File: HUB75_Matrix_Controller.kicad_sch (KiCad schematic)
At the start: 61 parts, among them J1 USB_C_Receptacle_USB2.0_16P, J2 Barrel_Jack_MountingPin, J3 Screw_Terminal_01x02, J4 Micro_SD_Card_Det2, J5 SFH11-PBPC-D08-ST-BK, SW1 EN, SW2 BOOT, U1 LSM6DSOTR, U2 AMS1117-3.3, U3 USBLC6-2SC6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

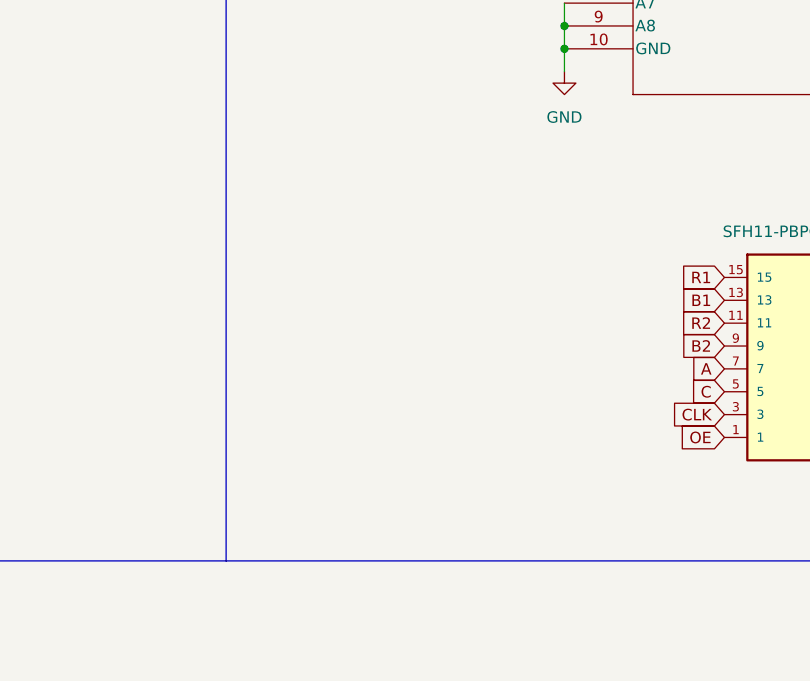
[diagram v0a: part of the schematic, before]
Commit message: ESP -> HUB75
Option to ignore Level Shifter
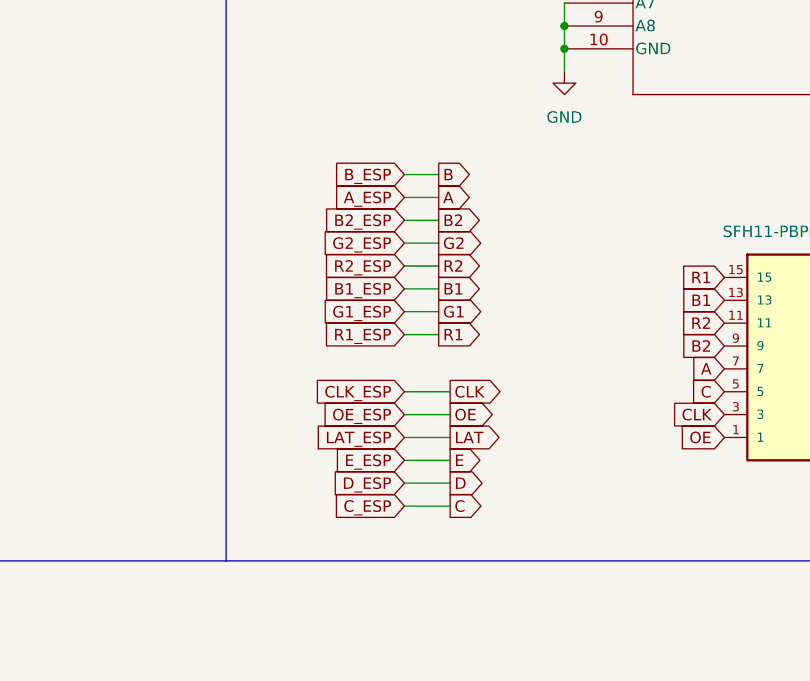
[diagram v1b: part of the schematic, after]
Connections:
- net A_ESP is gone; now on net A: U6.12 (GPIO7/ADC1_CH6), U7.3 (A2)
- net B1_ESP is gone; now on net B1: U6.8 (GPIO3/ADC1_CH2), U7.7 (A6)
- net B2_ESP is gone; now on net B2: U6.11 (GPIO6/ADC1_CH5), U7.4 (A3)
- net B_ESP is gone; now on net B: U6.13 (GPIO8/ADC1_CH7), U7.2 (A1)
- net CLK_ESP is gone; now on net CLK: U6.19 (GPIO14/ADC2_CH3), U8.2 (A1)
- net C_ESP is gone; now on net C: U6.14 (GPIO9/ADC1_CH8), U8.7 (A6)
- net D_ESP is gone; now on net D: U6.15 (GPIO10/ADC1_CH9), U8.6 (A5)
- net E_ESP is gone; now on net E: U6.16 (GPIO11/ADC2_CH0), U8.5 (A4)
- net G1_ESP is gone; now on net G1: U6.7 (GPIO2/ADC1_CH1), U7.8 (A7)
- net G2_ESP is gone; now on net G2: U6.10 (GPIO5/ADC1_CH4), U7.5 (A4)
- net LAT_ESP is gone; now on net LAT: U6.17 (GPIO12/ADC2_CH1), U8.4 (A3)
- net OE_ESP is gone; now on net OE: U6.18 (GPIO13/ADC2_CH2), U8.3 (A2)
- net R1_ESP is gone; now on net R1: U6.6 (GPIO1/ADC1_CH0), U7.9 (A8)
- net R2_ESP is gone; now on net R2: U6.9 (GPIO4/ADC1_CH3), U7.6 (A5)

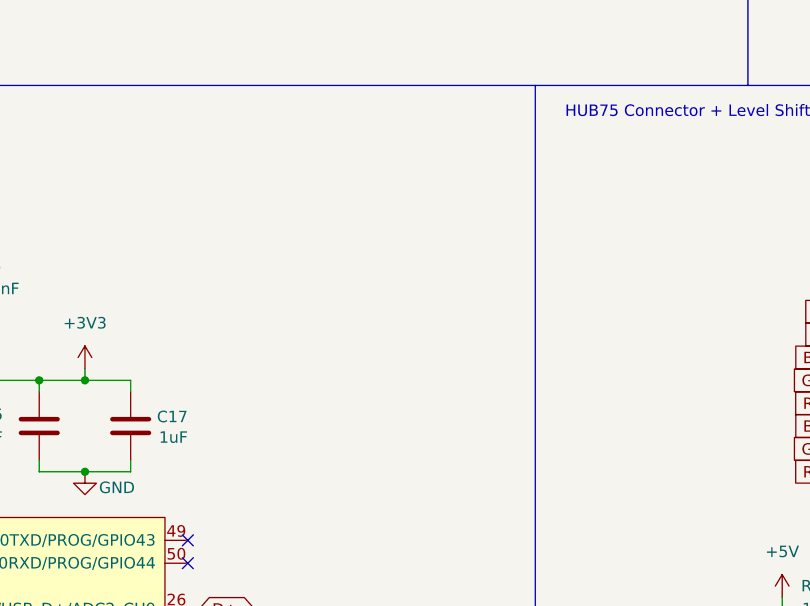
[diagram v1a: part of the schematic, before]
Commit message: Silkscreen Updates
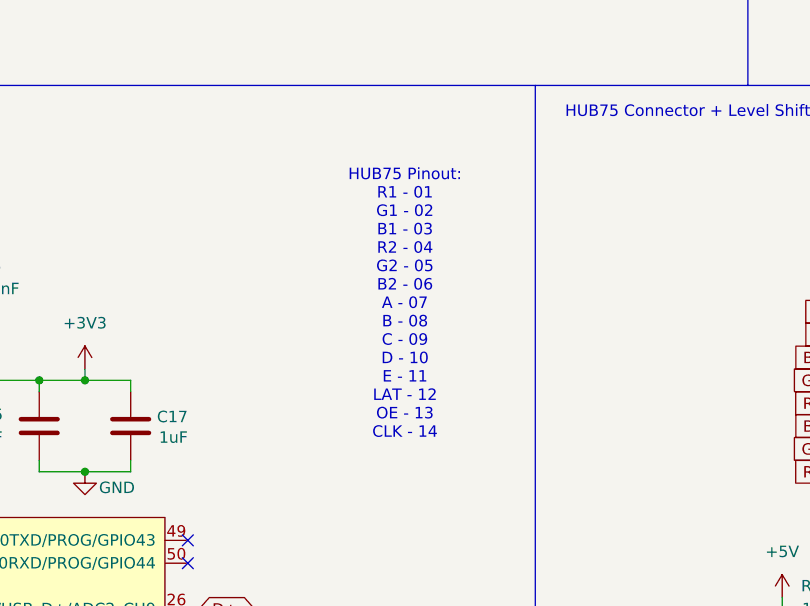
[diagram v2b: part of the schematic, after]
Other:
- note added: "HUB75 Pinout: R1 - 01 G1 - 02 B1 - 03 R2 - 04 G2 - 05 B2 - 06 A - 07 B - 08 C - 09 D - 10 E - 11 LAT - 12 OE - 13 CLK - 14"
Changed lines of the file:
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@@
+		)
+	)
+	(text "HUB75 Pinout:\nR1 - 01\nG1 - 02\nB1 - 03\nR2 - 04\nG2 - 05\nB2 - 06\nA - 07\nB - 08\nC - 09\nD - 10\nE - 11\nLAT - 12\nOE - 13\nCLK - 14\n"
+		(exclude_from_sim no)
+		(at 271.78 84.328 0)
+		(effects
+			(font
+				(size 1.27 1.27)
+			)
 		)
 	)

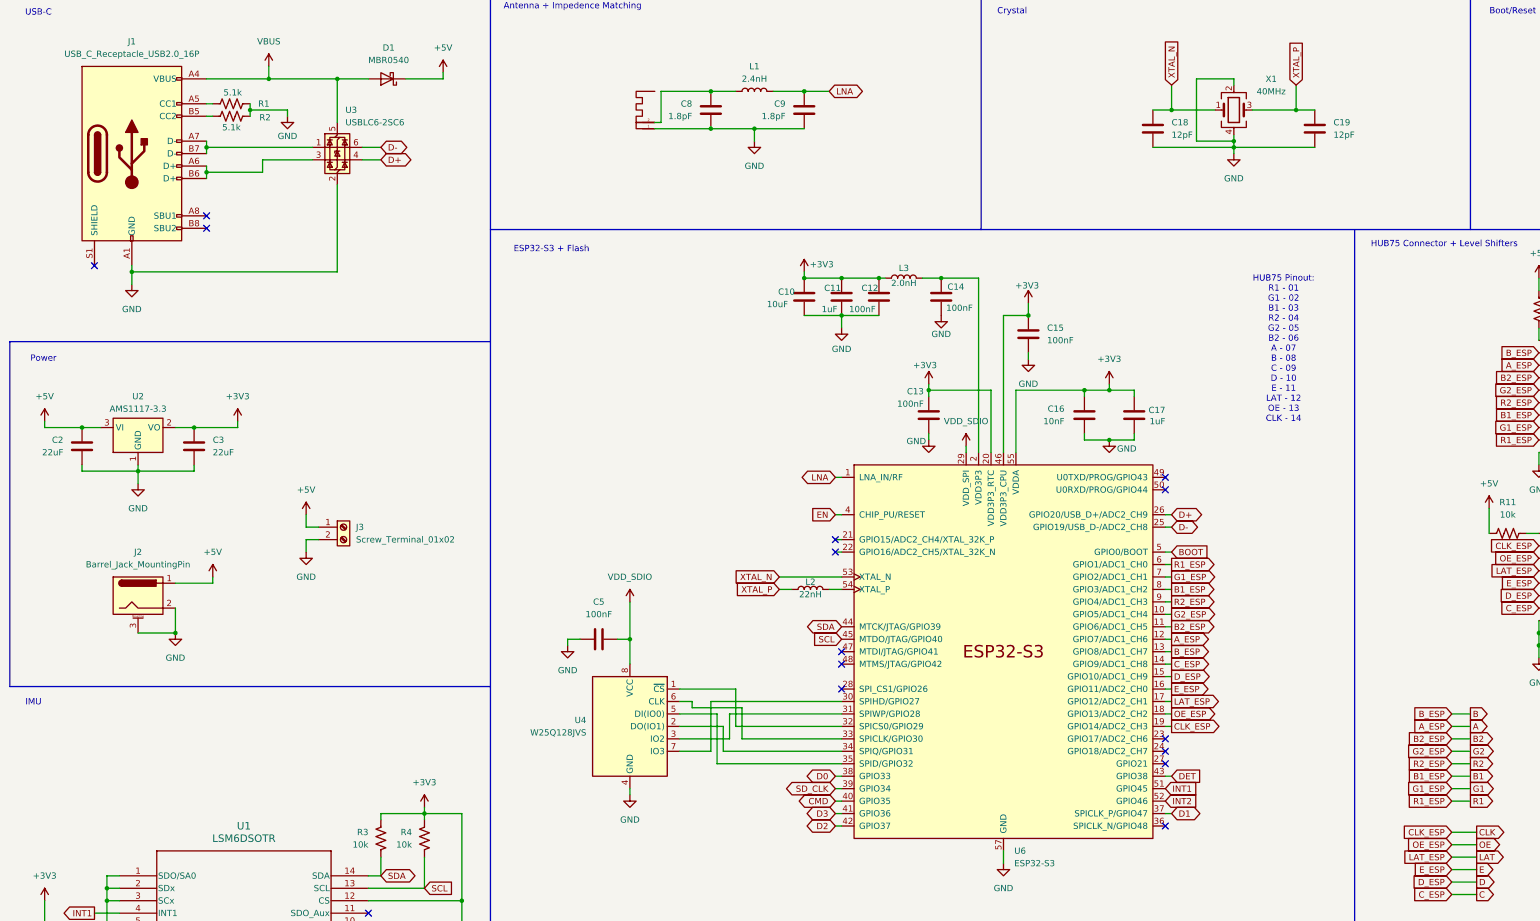
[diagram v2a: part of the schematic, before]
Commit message: v2, fixed SD and USB
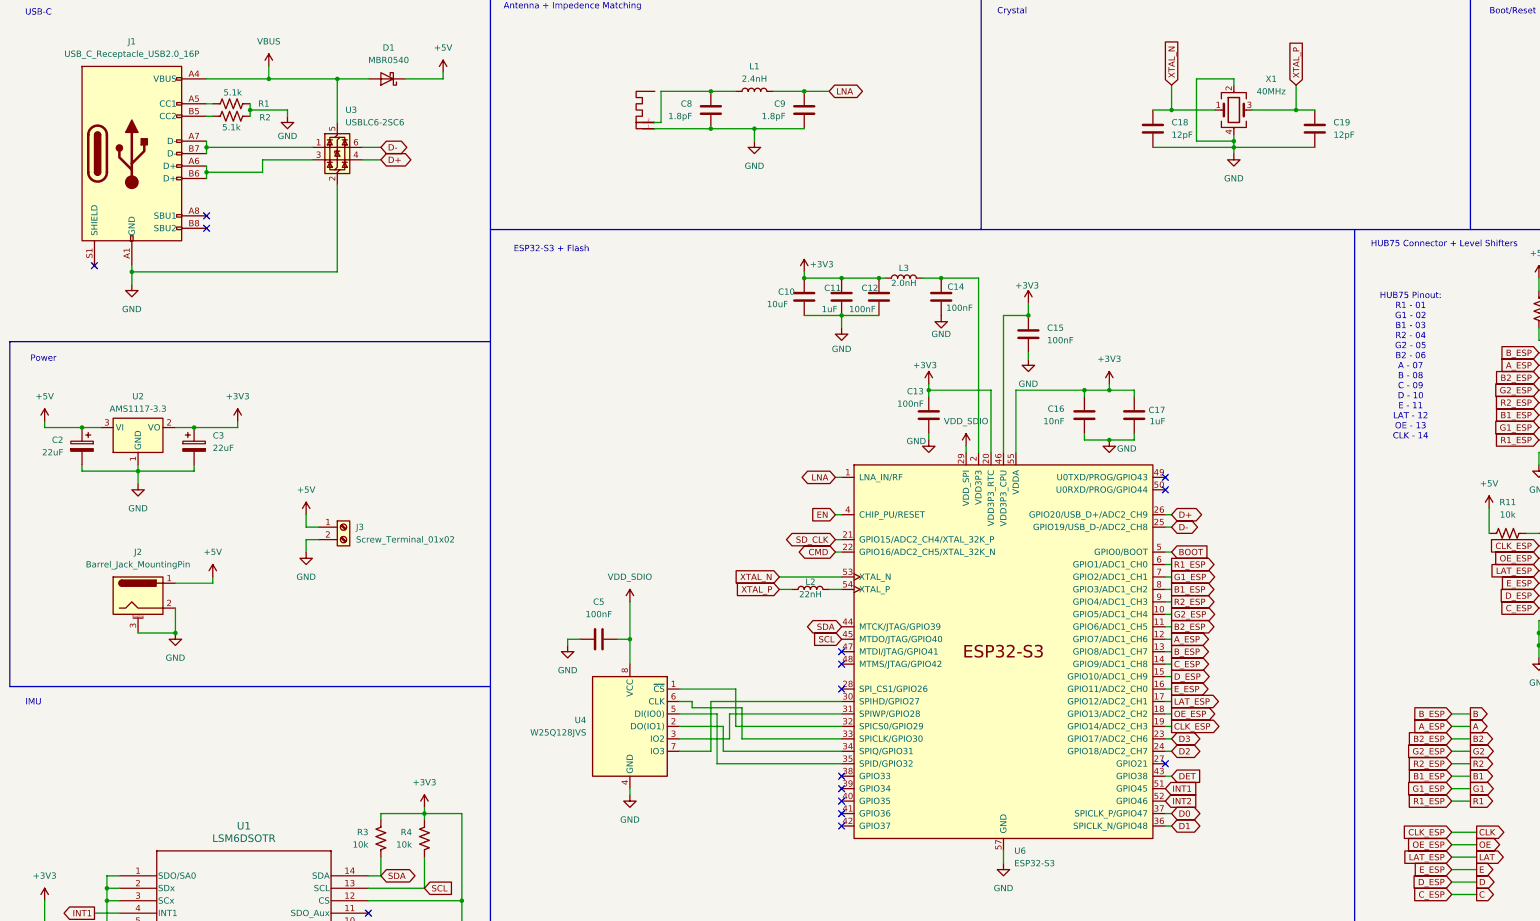
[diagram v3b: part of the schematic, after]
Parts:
- C2, C3: symbol Device:C -> Device:C_Polarized
- J5: footprint Project Footprints:SULLINS_SFH11-PBPC-D08-ST-BK -> footprints:SULLINS_SFH11-PBPC-D08-ST-BK
- U1: footprint Project Footprints:LGA-14L_2P5X3X0P86_STM -> footprints:LGA-14L_2P5X3X0P86_STM
- U7, U8: footprint Project Footprints:PW20 -> footprints:PW20
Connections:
- net CMD: now also U6.22 (GPIO16/ADC2_CH5/XTAL_32K_N); no longer U6.40 (GPIO35)
- net D0: now also U6.37 (SPICLK_P/GPIO47); no longer U6.38 (GPIO33)
- net D1: now also U6.36 (SPICLK_N/GPIO48); no longer U6.37 (SPICLK_P/GPIO47)
- net D2: now also U6.24 (GPIO18/ADC2_CH7); no longer U6.42 (GPIO37)
- net D3: now also U6.23 (GPIO17/ADC2_CH6); no longer U6.41 (GPIO36)
- net SD_CLK: now also U6.21 (GPIO15/ADC2_CH4/XTAL_32K_P); no longer U6.39 (GPIO34)

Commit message: v1.1, final changes
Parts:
- C22, C23, C24, C25, R11, R12, R15, R16, U7, U8: now not fitted; now left out of the parts list
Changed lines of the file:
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@@
 		(unit 1)
 		(exclude_from_sim no)
-		(in_bom yes)
-		(on_board yes)
-		(dnp no)
+		(in_bom no)
+		(on_board no)
+		(dnp yes)
 		(property "Reference" "C25"
 			(at 392.684 113.792 0)
@@
 		(unit 1)
 		(exclude_from_sim no)
-		(in_bom yes)
-		(on_board yes)
-		(dnp no)
+		(in_bom no)
+		(on_board no)
+		(dnp yes)
 		(fields_autoplaced yes)
 		(property "Reference" "U8"
@@
 		(unit 1)
 		(exclude_from_sim no)
-		(in_bom yes)
-		(on_board yes)
-		(dnp no)
+		(in_bom no)
+		(on_board no)
+		(dnp yes)
 		(property "Reference" "C22"
 			(at 382.524 69.342 0)
@@
 		(unit 1)
 		(exclude_from_sim no)
-		(in_bom yes)
-		(on_board yes)
-		(dnp no)
+		(in_bom no)
+		(on_board no)
+		(dnp yes)
 		(fields_autoplaced yes)
 		(property "Reference" "R12"
@@
 		(unit 1)
 		(exclude_from_sim no)
-		(in_bom yes)
-		(on_board yes)
-		(dnp no)
+		(in_bom no)
+		(on_board no)
+		(dnp yes)
 		(property "Reference" "R16"
 			(at 388.62 130.81 90)
@@
 		(unit 1)
 		(exclude_from_sim no)
-		(in_bom yes)
-		(on_board yes)
-		(dnp no)
+		(in_bom no)
+		(on_board no)
+		(dnp yes)
 		(fields_autoplaced yes)
 		(property "Reference" "U7"
@@
 		(unit 1)
 		(exclude_from_sim no)
-		(in_bom yes)
-		(on_board yes)
-		(dnp no)
+		(in_bom no)
+		(on_board no)
+		(dnp yes)
 		(fields_autoplaced yes)
 		(property "Reference" "R11"
@@
 		(unit 1)
 		(exclude_from_sim no)
-		(in_bom yes)
-		(on_board yes)
-		(dnp no)
+		(in_bom no)
+		(on_board no)
+		(dnp yes)
 		(fields_autoplaced yes)
 		(property "Reference" "R15"
@@
 		(unit 1)
 		(exclude_from_sim no)
-		(in_bom yes)
-		(on_board yes)
-		(dnp no)
+		(in_bom no)
+		(on_board no)
+		(dnp yes)
 		(property "Reference" "C23"
 			(at 385.064 113.792 0)
@@
 		(unit 1)
 		(exclude_from_sim no)
-		(in_bom yes)
-		(on_board yes)
-		(dnp no)
+		(in_bom no)
+		(on_board no)
+		(dnp yes)
 		(property "Reference" "C24"
 			(at 390.144 69.342 0)
